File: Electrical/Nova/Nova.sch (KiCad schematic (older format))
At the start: 14 parts, among them SW1 SW_Push, SW2 SW_Push, U1 STM32F411CEUx

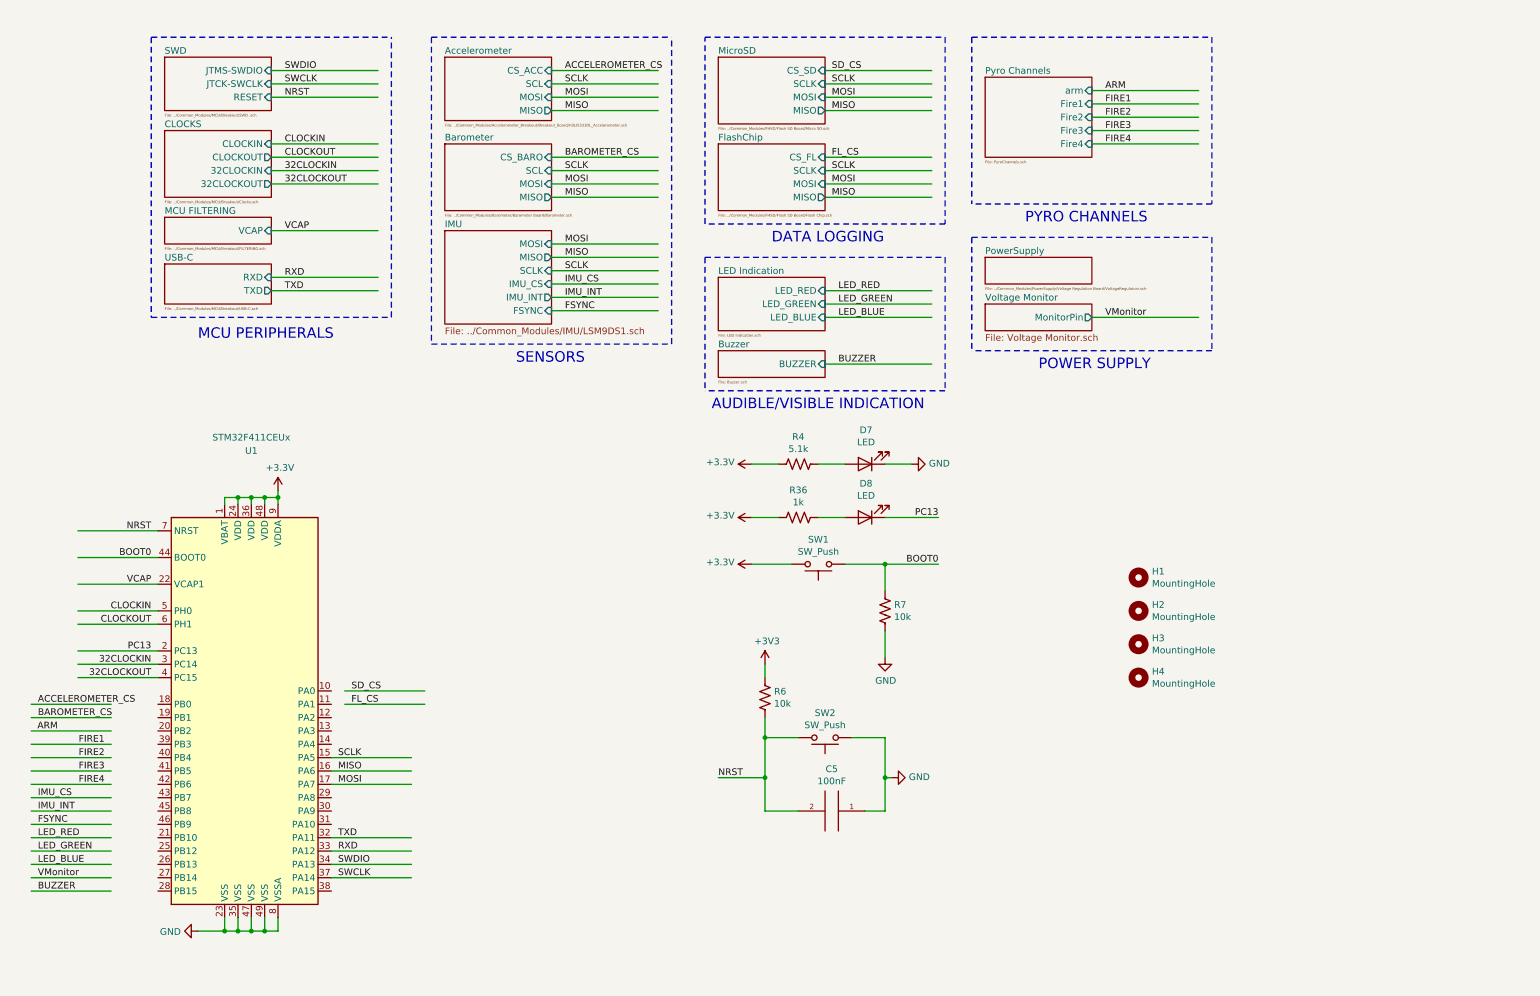
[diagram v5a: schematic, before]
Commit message: Changes to PCB Layout Getting Closer to Final Form
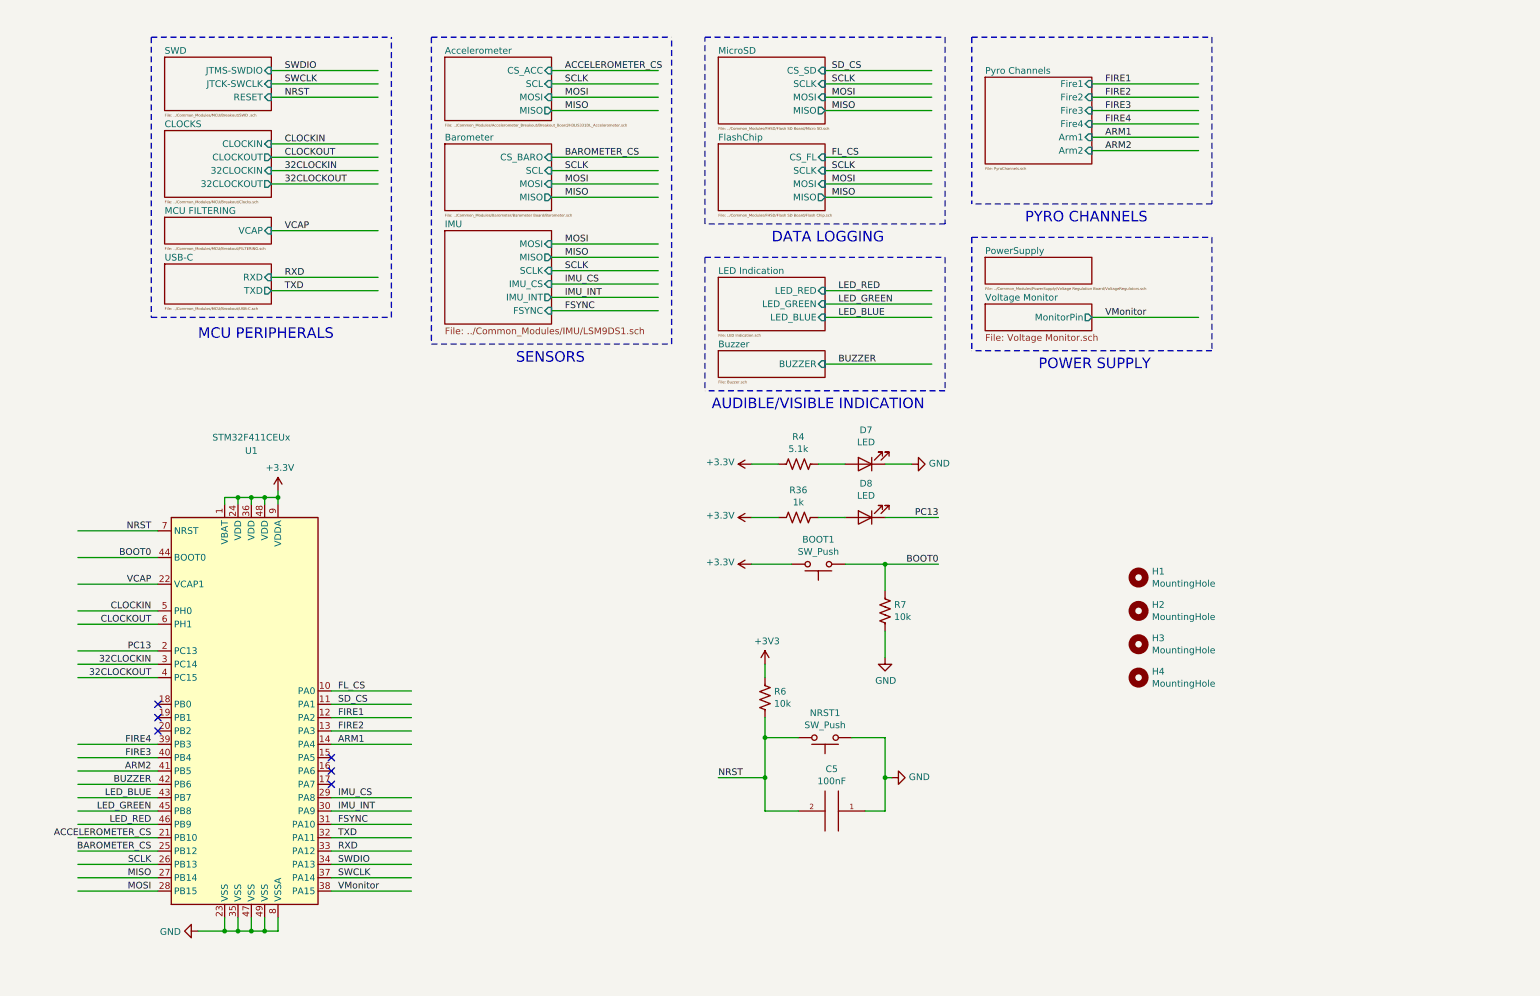
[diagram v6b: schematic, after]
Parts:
- renumbered SW1 to BOOT1, SW2 to NRST1
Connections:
- net labels added: ARM1, ARM2
- net labels removed: ARM
- wire segments 117 -> 119
- no-connect marks 0 -> 6
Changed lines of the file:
@@
 Text Notes 8100 2150 0    79   ~ 0
 PYRO CHANNELS
-Text Label 8700 1450 0    50   ~ 0
+Text Label 8700 1300 0    50   ~ 0
 FIRE3
 $Sheet
-S 7800 1050 800  600
+S 7800 1050 800  650
 U 5F448D4B
 F0 "Pyro Channels" 50
 F1 "PyroChannels.sch" 20
-F2 "arm" I R 8600 1150 50
-F3 "Fire1" I R 8600 1250 50
-F4 "Fire2" I R 8600 1350 50
-F5 "Fire3" I R 8600 1450 50
-F6 "Fire4" I R 8600 1550 50
+F2 "Fire1" I R 8600 1100 50
+F3 "Fire2" I R 8600 1200 50
+F4 "Fire3" I R 8600 1300 50
+F5 "Fire4" I R 8600 1400 50
+F6 "Arm1" I R 8600 1500 50
+F7 "Arm2" I R 8600 1600 50
 $EndSheet
-Text Label 8700 1350 0    50   ~ 0
+Text Label 8700 1200 0    50   ~ 0
 FIRE2
-Text Label 8700 1250 0    50   ~ 0
+Text Label 8700 1100 0    50   ~ 0
 FIRE1
-Text Label 8700 1150 0    50   ~ 0
-ARM
-Wire Wire Line
-	8600 1150 9400 1150
-Wire Wire Line
-	8600 1250 9400 1250
-Wire Wire Line
-	8600 1350 9400 1350
-Wire Wire Line
-	8600 1450 9400 1450
+Text Label 8700 1500 0    50   ~ 0
+ARM1
+Wire Wire Line
+	8600 1500 9400 1500
+Wire Wire Line
+	8600 1100 9400 1100
+Wire Wire Line
+	8600 1200 9400 1200
+Wire Wire Line
+	8600 1300 9400 1300
 Wire Notes Line
 	1550 750  3350 750
@@
 	1600 4850 1000 4850
 Wire Wire Line
-	1250 7150 650  7150
-Wire Wire Line
-	1250 6950 650  6950
-Wire Wire Line
-	1250 6850 650  6850
-Wire Wire Line
-	1250 6750 650  6750
-Wire Wire Line
 	3500 6950 2900 6950
 Wire Wire Line
@@
 	3500 6750 2900 6750
 Wire Wire Line
-	2900 6150 3500 6150
-Wire Wire Line
-	2900 6250 3500 6250
-Wire Wire Line
-	2900 6350 3500 6350
-Text Label 8700 1550 0    50   ~ 0
+	1600 6950 1000 6950
+Wire Wire Line
+	1600 7050 1000 7050
+Wire Wire Line
+	1600 7150 1000 7150
+Text Label 8700 1400 0    50   ~ 0
 FIRE4
 Wire Wire Line
-	8600 1550 9400 1550
+	8600 1400 9400 1400
 Wire Notes Line
 	9500 750  9500 2000
@@
 Text Notes 6200 2300 0    79   ~ 0
 DATA LOGGING\n
-Text Label 2950 6250 0    50   ~ 0
+Text Label 1550 7050 2    50   ~ 0
 MISO
-Text Label 2950 6350 0    50   ~ 0
+Text Label 1550 7150 2    50   ~ 0
 MOSI
-Text Label 2950 6150 0    50   ~ 0
+Text Label 1550 6950 2    50   ~ 0
 SCLK
 Text Label 1550 4850 2    50   ~ 0
@@
 Text Label 2950 6950 0    50   ~ 0
 SWDIO
-Text Label 700  6750 0    50   ~ 0
-LED_RED
-Text Label 700  6850 0    50   ~ 0
-LED_GREEN
-Text Label 700  6950 0    50   ~ 0
-LED_BLUE
-Text Label 700  7150 0    50   ~ 0
-BUZZER
-Text Label 850  5950 2    50   ~ 0
-ARM
 Text Label 4650 1650 0    50   ~ 0
 BAROMETER_CS
@@
 	1    0    0    -1
 $EndComp
-Text Label 700  7050 0    50   ~ 0
-VMonitor
-Wire Wire Line
-	1250 7050 650  7050
-Text Label 3050 5750 0    50   ~ 0
+Text Label 2950 5650 0    50   ~ 0
 FL_CS
 Wire Wire Line
-	650  5950 1250 5950
-Wire Wire Line
-	650  5850 1250 5850
-Wire Wire Line
-	3600 5750 3000 5750
-Wire Wire Line
-	3000 5650 3600 5650
-Wire Wire Line
-	650  5750 1250 5750
-Text Label 3050 5650 0    50   ~ 0
+	3500 5650 2900 5650
+Wire Wire Line
+	2900 5750 3500 5750
+Text Label 2950 5750 0    50   ~ 0
 SD_CS
-Text Label 700  5850 0    50   ~ 0
-BAROMETER_CS
-Text Label 700  5750 0    50   ~ 0
-ACCELEROMETER_CS
 Text Label 6650 1750 0    50   ~ 0
 SCLK
@@
 $EndComp
 $Comp
-L Switch:SW_Push SW1
+L Switch:SW_Push BOOT1
 U 1 1 61C94220
 P 6550 4700
-F 0 "SW1" H 6550 4515 50  0000 C CNN
+F 0 "BOOT1" H 6550 4515 50  0000 C CNN
 F 1 "SW_Push" H 6550 4606 50  0000 C CNN
 F 2 "NOVA MCU (STM):KSR223GLFG" H 6550 4900 50  0001 C CNN
@@
 $EndComp
 $Comp
-L Switch:SW_Push SW2
+L Switch:SW_Push NRST1
 U 1 1 61CFD677
 P 6600 6000
-F 0 "SW2" H 6600 5815 50  0000 C CNN
+F 0 "NRST1" H 6600 5815 50  0000 C CNN
 F 1 "SW_Push" H 6600 5906 50  0000 C CNN
 F 2 "NOVA MCU (STM):KSR223GLFG" H 6600 6200 50  0001 C CNN
@@
 Text Label 4650 2800 0    50   ~ 0
 FSYNC
-Text Label 700  6450 0    50   ~ 0
-IMU_CS
-Text Label 700  6550 0    50   ~ 0
-IMU_INT
-Text Label 700  6650 0    50   ~ 0
-FSYNC
 Wire Notes Line
 	5450 3050 5450 750
 Wire Notes Line
 	3650 750  3650 3050
-Wire Wire Line
-	1250 6650 650  6650
-Wire Wire Line
-	1250 6550 650  6550
-Wire Wire Line
-	1250 6450 650  6450
 Wire Wire Line
 	2200 4200 2100 4200
 Connection ~ 2200 4200
-Text Label 1200 6350 2    50   ~ 0
-FIRE4
-Text Label 1200 6250 2    50   ~ 0
-FIRE3
-Text Label 1200 6150 2    50   ~ 0
-FIRE2
-Wire Wire Line
-	650  6250 1250 6250
-Wire Wire Line
-	1250 6150 650  6150
-Wire Wire Line
-	1250 6050 650  6050
-Text Label 1200 6050 2    50   ~ 0
-FIRE1
-Wire Wire Line
-	650  6350 1250 6350
 Text Label 7450 4350 2    50   ~ 0
 PC13
@@
 	0    1    1    0
 $EndComp
+Wire Wire Line
+	1000 6050 1600 6050
+Text Label 2950 5850 0    50   ~ 0
+FIRE1
+Wire Wire Line
+	2900 5850 3500 5850
+Wire Wire Line
+	2900 5950 3500 5950
+Wire Wire Line
+	1600 6150 1000 6150
+Text Label 2950 5950 0    50   ~ 0
+FIRE2
+Text Label 1550 6150 2    50   ~ 0
+FIRE3
+Text Label 1550 6050 2    50   ~ 0
+FIRE4
+Wire Wire Line
+	3500 6450 2900 6450
+Wire Wire Line
+	3500 6550 2900 6550
+Wire Wire Line
+	3500 6650 2900 6650
+Text Label 2950 6650 0    50   ~ 0
+FSYNC
+Text Label 2950 6550 0    50   ~ 0
+IMU_INT
+Text Label 2950 6450 0    50   ~ 0
+IMU_CS
+Text Label 1550 6750 2    50   ~ 0
+ACCELEROMETER_CS
+Text Label 1550 6850 2    50   ~ 0
+BAROMETER_CS
+Wire Wire Line
+	1600 6750 1000 6750
+Wire Wire Line
+	1600 6850 1000 6850
+Wire Wire Line
+	2900 6050 3500 6050
+Wire Wire Line
+	3500 7150 2900 7150
+Text Label 2950 7150 0    50   ~ 0
+VMonitor
+Text Label 2950 6050 0    50   ~ 0
+ARM1
+Text Label 1550 6350 2    50   ~ 0
+BUZZER
+Text Label 1550 6450 2    50   ~ 0
+LED_BLUE
+Text Label 1550 6550 2    50   ~ 0
+LED_GREEN
+Text Label 1550 6650 2    50   ~ 0
+LED_RED
+Wire Wire Line
+	1000 6650 1600 6650
+Wire Wire Line
+	1000 6550 1600 6550
+Wire Wire Line
+	1000 6450 1600 6450
+Wire Wire Line
+	1000 6350 1600 6350
+Text Label 8700 1600 0    50   ~ 0
+ARM2
+Wire Wire Line
+	8600 1600 9400 1600
+Wire Wire Line
+	1600 6250 1000 6250
+Text Label 1550 6250 2    50   ~ 0
+ARM2
+NoConn ~ 2900 6350
+NoConn ~ 2900 6250
+NoConn ~ 2900 6150
+NoConn ~ 1600 5950
+NoConn ~ 1600 5850
+NoConn ~ 1600 5750
 $EndSCHEMATC

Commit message: Silkscreen Cleanup
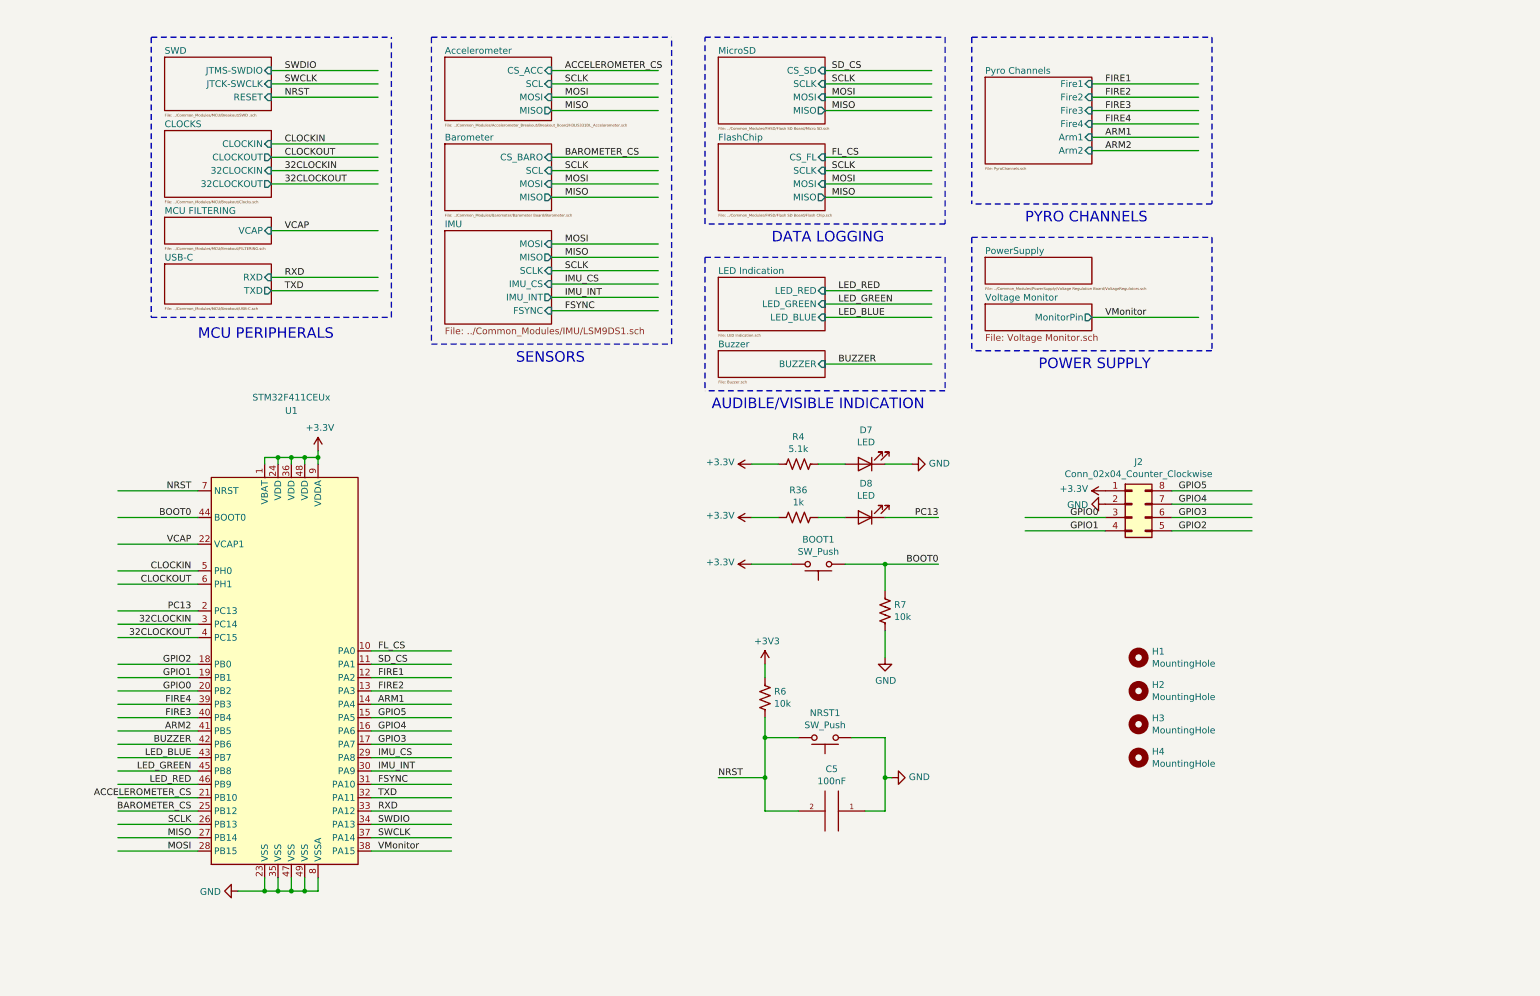
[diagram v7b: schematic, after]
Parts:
- added J2: Conn_02x04_Counter_Clockwise, Connector_PinSocket_2.54mm:PinSocket_2x04_P2.54mm_Vertical, symbol Connector_Generic:Conn_02x04_Counter_Clockwise
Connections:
- net labels added: GPIO0, GPIO1, GPIO2, GPIO3, GPIO4, GPIO5
- wire segments 119 -> 131
- no-connect marks 6 -> 0
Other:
- moved on the sheet: H1, H2, H3, H4, U1
